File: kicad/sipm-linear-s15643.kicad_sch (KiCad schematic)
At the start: 34 parts, among them J1 SSQ-103-01-G-D, U2 S15643

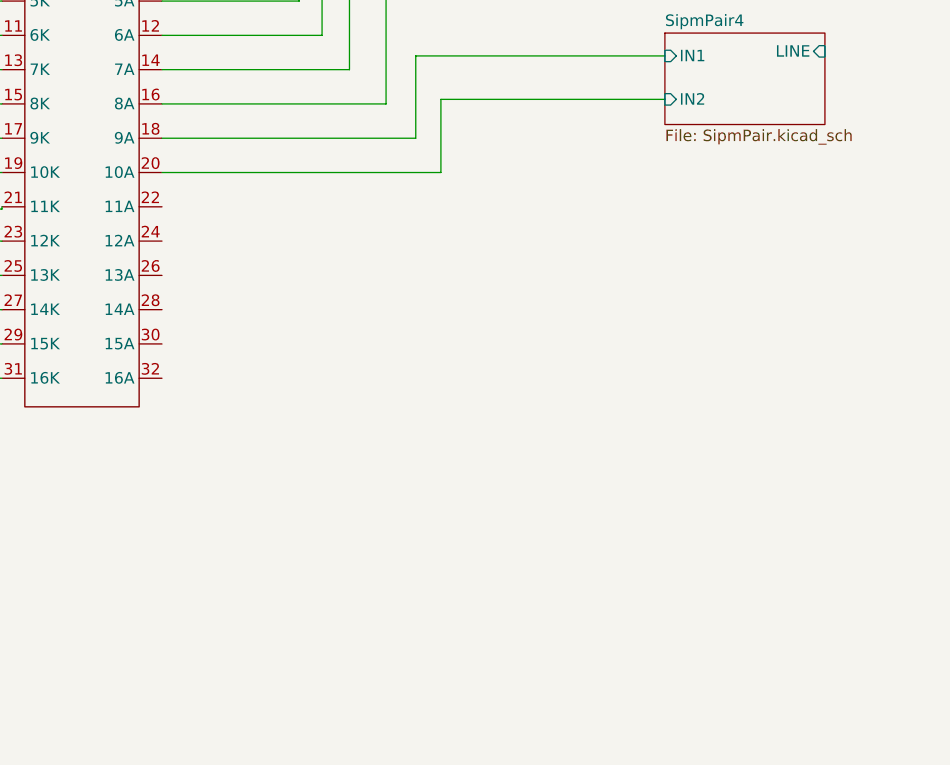
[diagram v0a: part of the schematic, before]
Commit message: Update layout for the new footprint
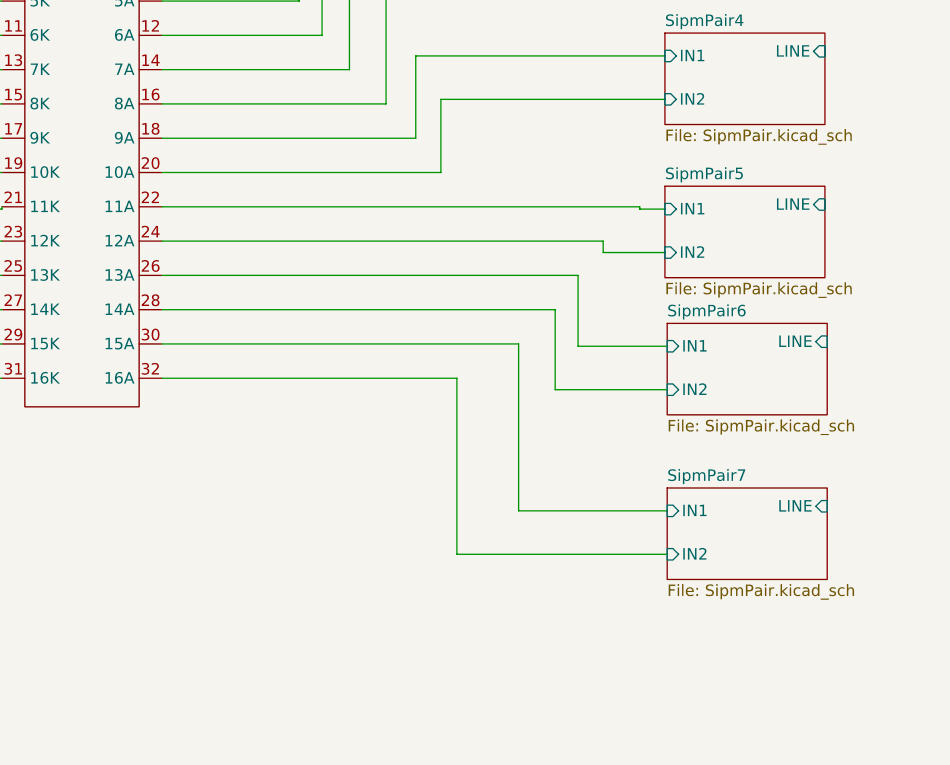
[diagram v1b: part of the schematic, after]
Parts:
- U2: footprint footprints:S15643-N16 -> S13615-1025:AF210729-S14160-x16
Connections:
- net SipmPair5/IN1: now reaches U2.22 (11A)
- net SipmPair5/IN2: now reaches U2.24 (12A)
- net SipmPair6/IN1: now reaches U2.26 (13A)
- net SipmPair6/IN2: now reaches U2.28 (14A)
- net SipmPair7/IN1: now reaches U2.30 (15A)
- net SipmPair7/IN2: now reaches U2.32 (16A)
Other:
- added sheet SipmPair5 (SipmPair.kicad_sch)
- added sheet SipmPair6 (SipmPair.kicad_sch)
- added sheet SipmPair7 (SipmPair.kicad_sch)

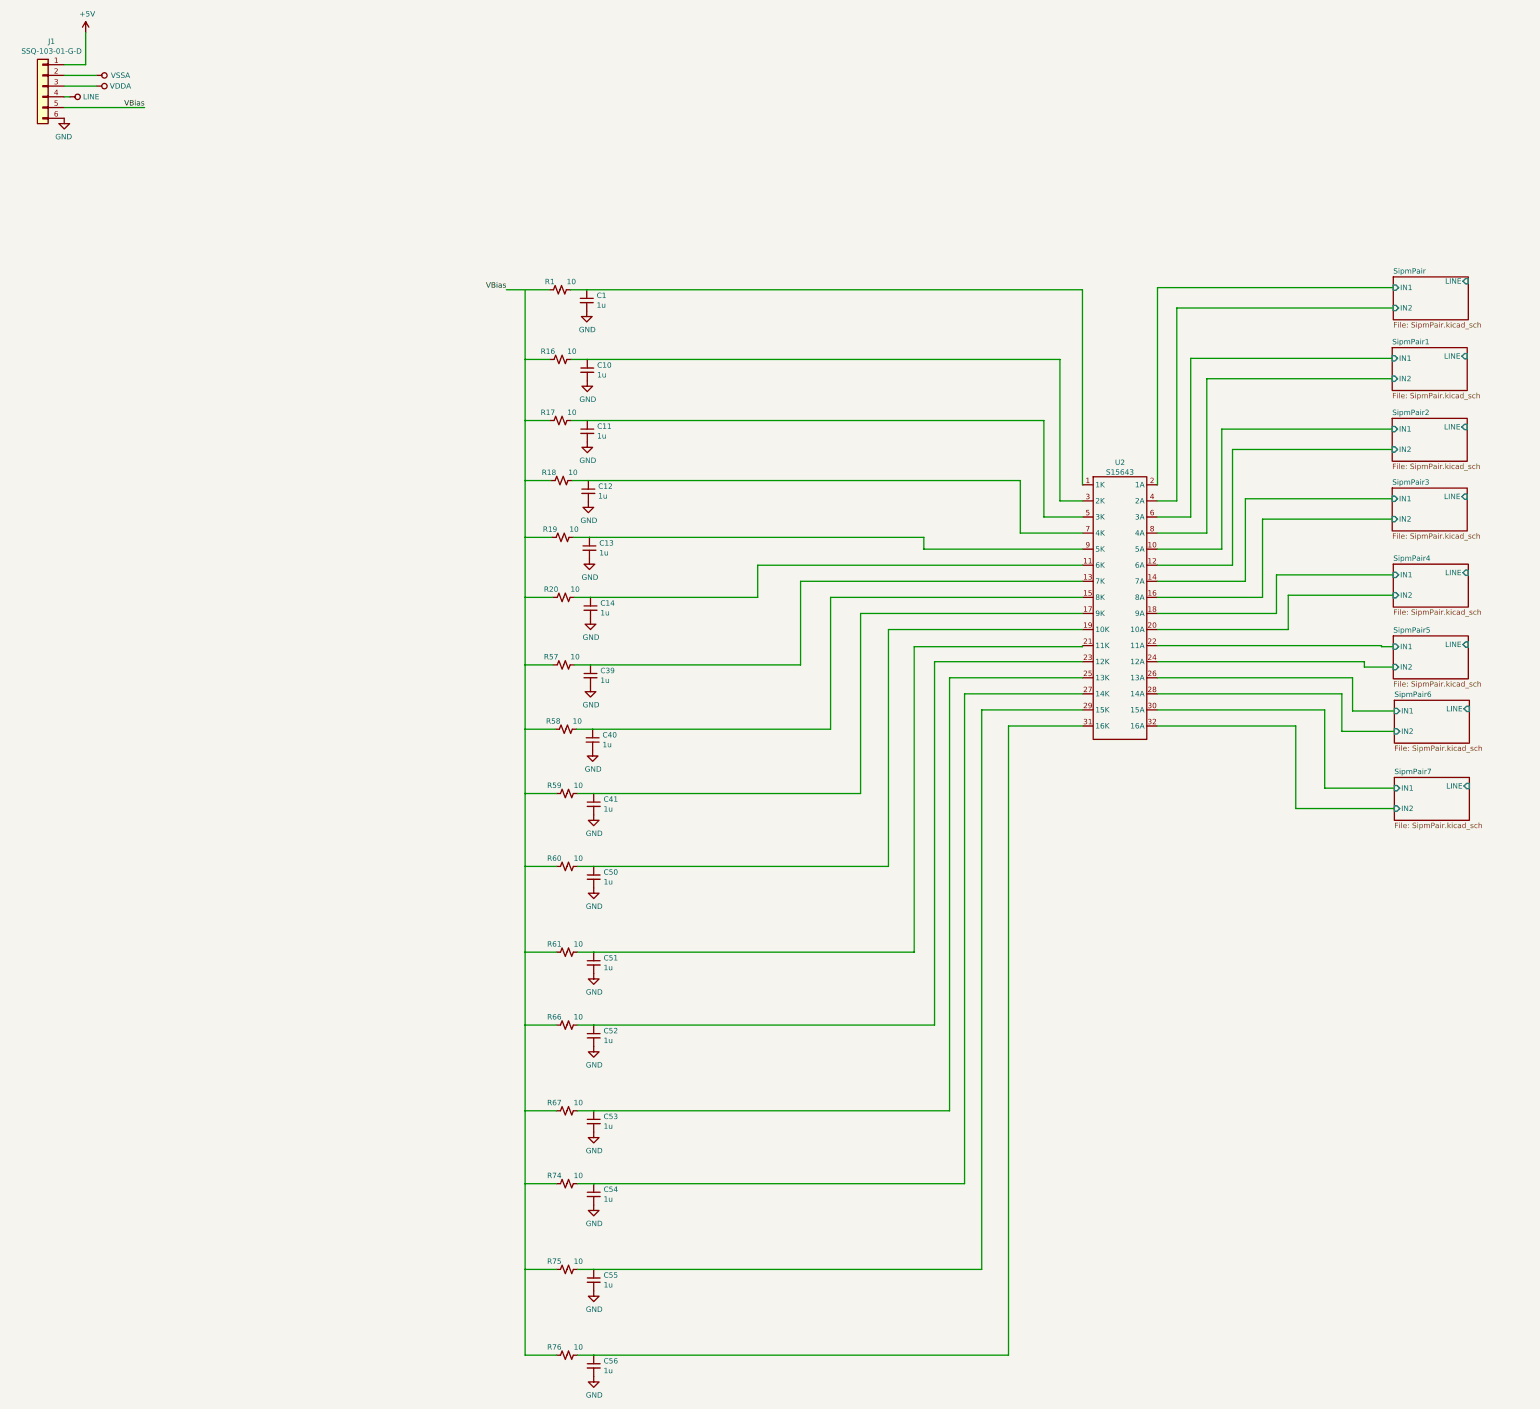
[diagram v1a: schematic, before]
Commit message: Update foot print for the revised hamamatsu part
They only have 2 cathode connections.  In addition, add a second power connector, since at least two power supplies are going to be needed.
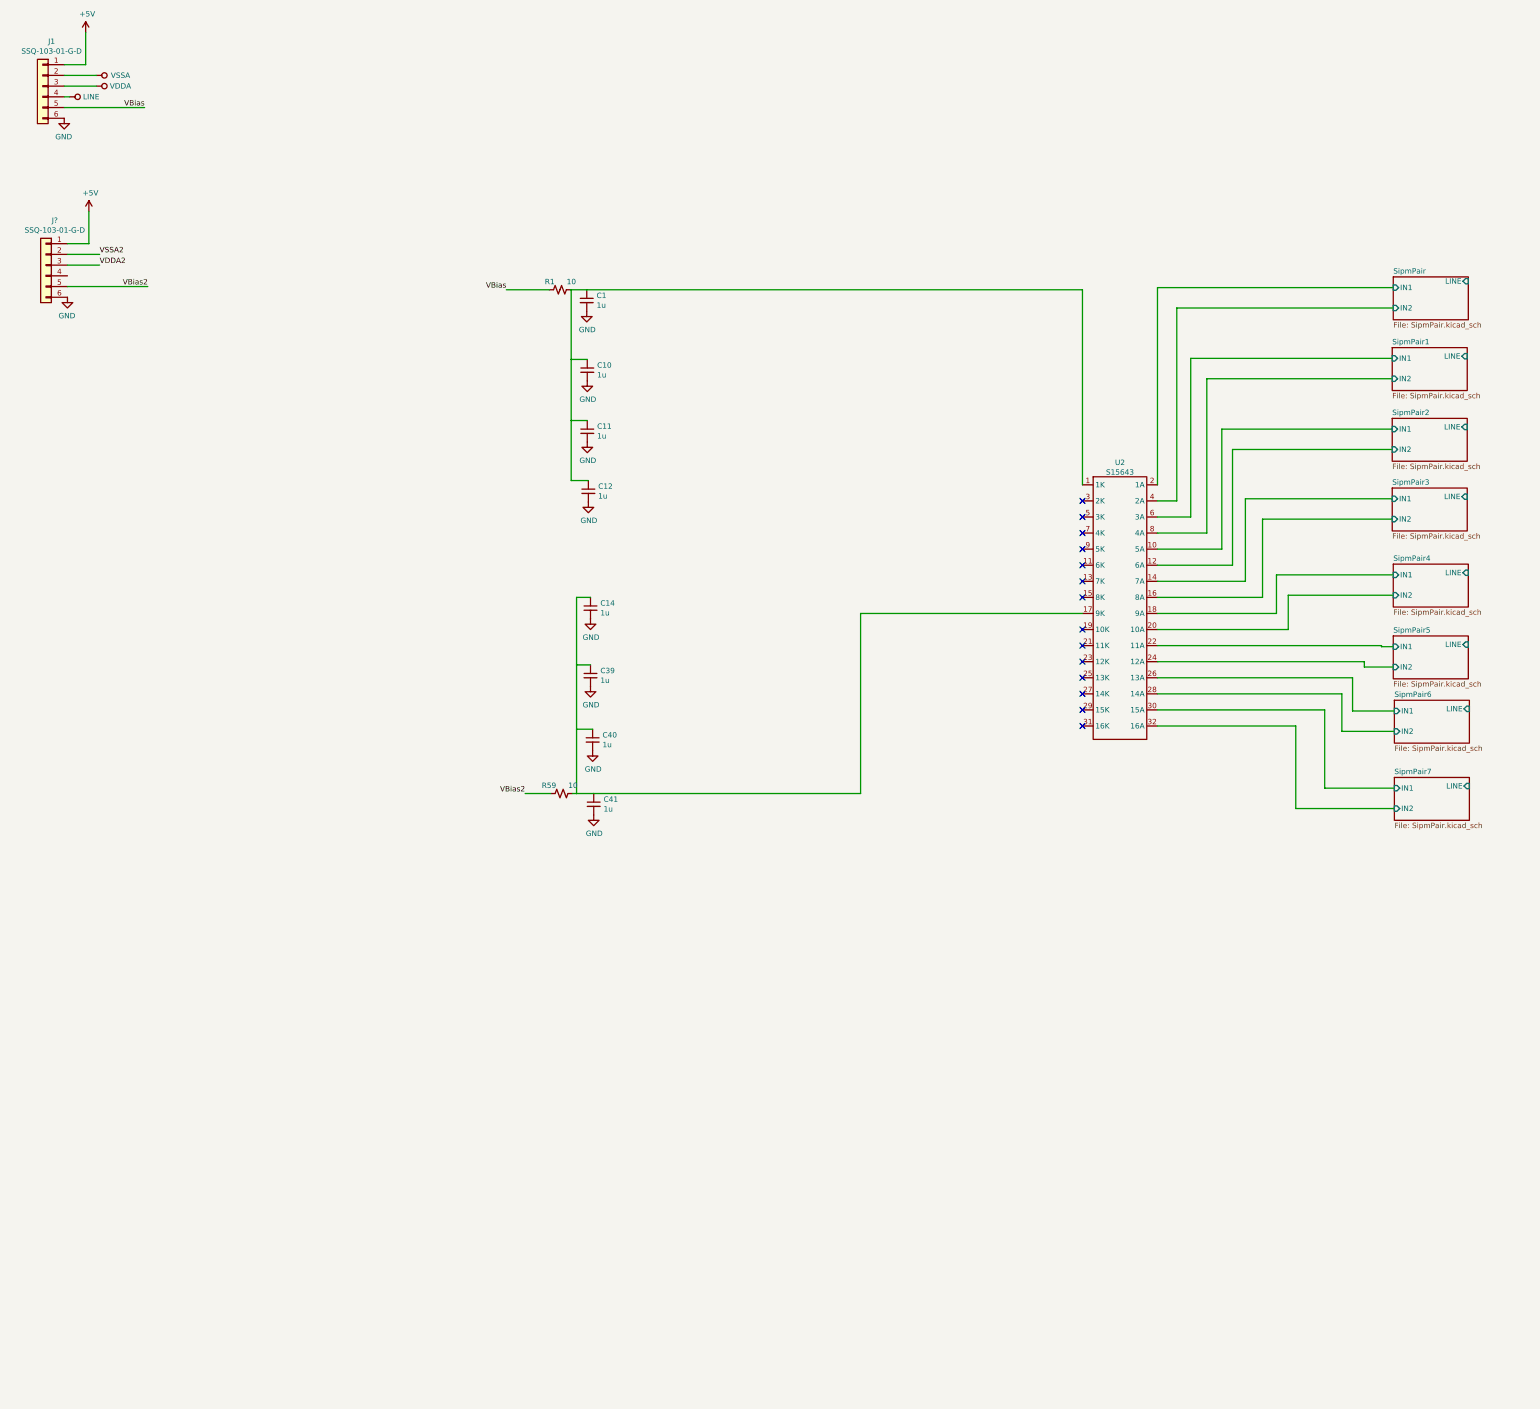
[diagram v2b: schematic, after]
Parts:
- removed C13, C50, C51, C52, C53, C54, C55, C56: 1u, Capacitor_SMD:C_0805_2012Metric, symbol Device:C_Small
- removed R16, R17, R18, R19, R20, R57, R58, R60, R61, R66, R67, R74, R75, R76: 10, R_0402_1005Metric, symbol Device:R_Small_US
- added J?: SSQ-103-01-G-D, footprints:PinHeader_2x03_P2.54mm_Vertical, symbol Connector_Generic:Conn_01x06
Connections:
- net +5V: now also J?.1 (Pin_1)
- net GND: now also J?.6 (Pin_6)
- net at C1.1, R1.2, U2.1 (1K): now also C10.1, C11.1, C12.1
- net at U2.11 (6K): no longer C14.1
- net at U2.13 (7K): no longer C39.1
- net at U2.15 (8K): no longer C40.1
- net at C41.1, R59.2, U2.17 (9K): now also C14.1, C39.1, C40.1
- net at U2.3 (2K): no longer C10.1
- net at U2.5 (3K): no longer C11.1
- net at U2.7 (4K): no longer C12.1
- net VBias2: now reaches R59.1
- net VBias2: now also J?.5 (Pin_5)
- new net VDDA2: J?.3 (Pin_3)
- new net VSSA2: J?.2 (Pin_2)
- no-connect marks 0 -> 14
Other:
- moved on the sheet: R59

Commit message: Split power rails across two power supplies
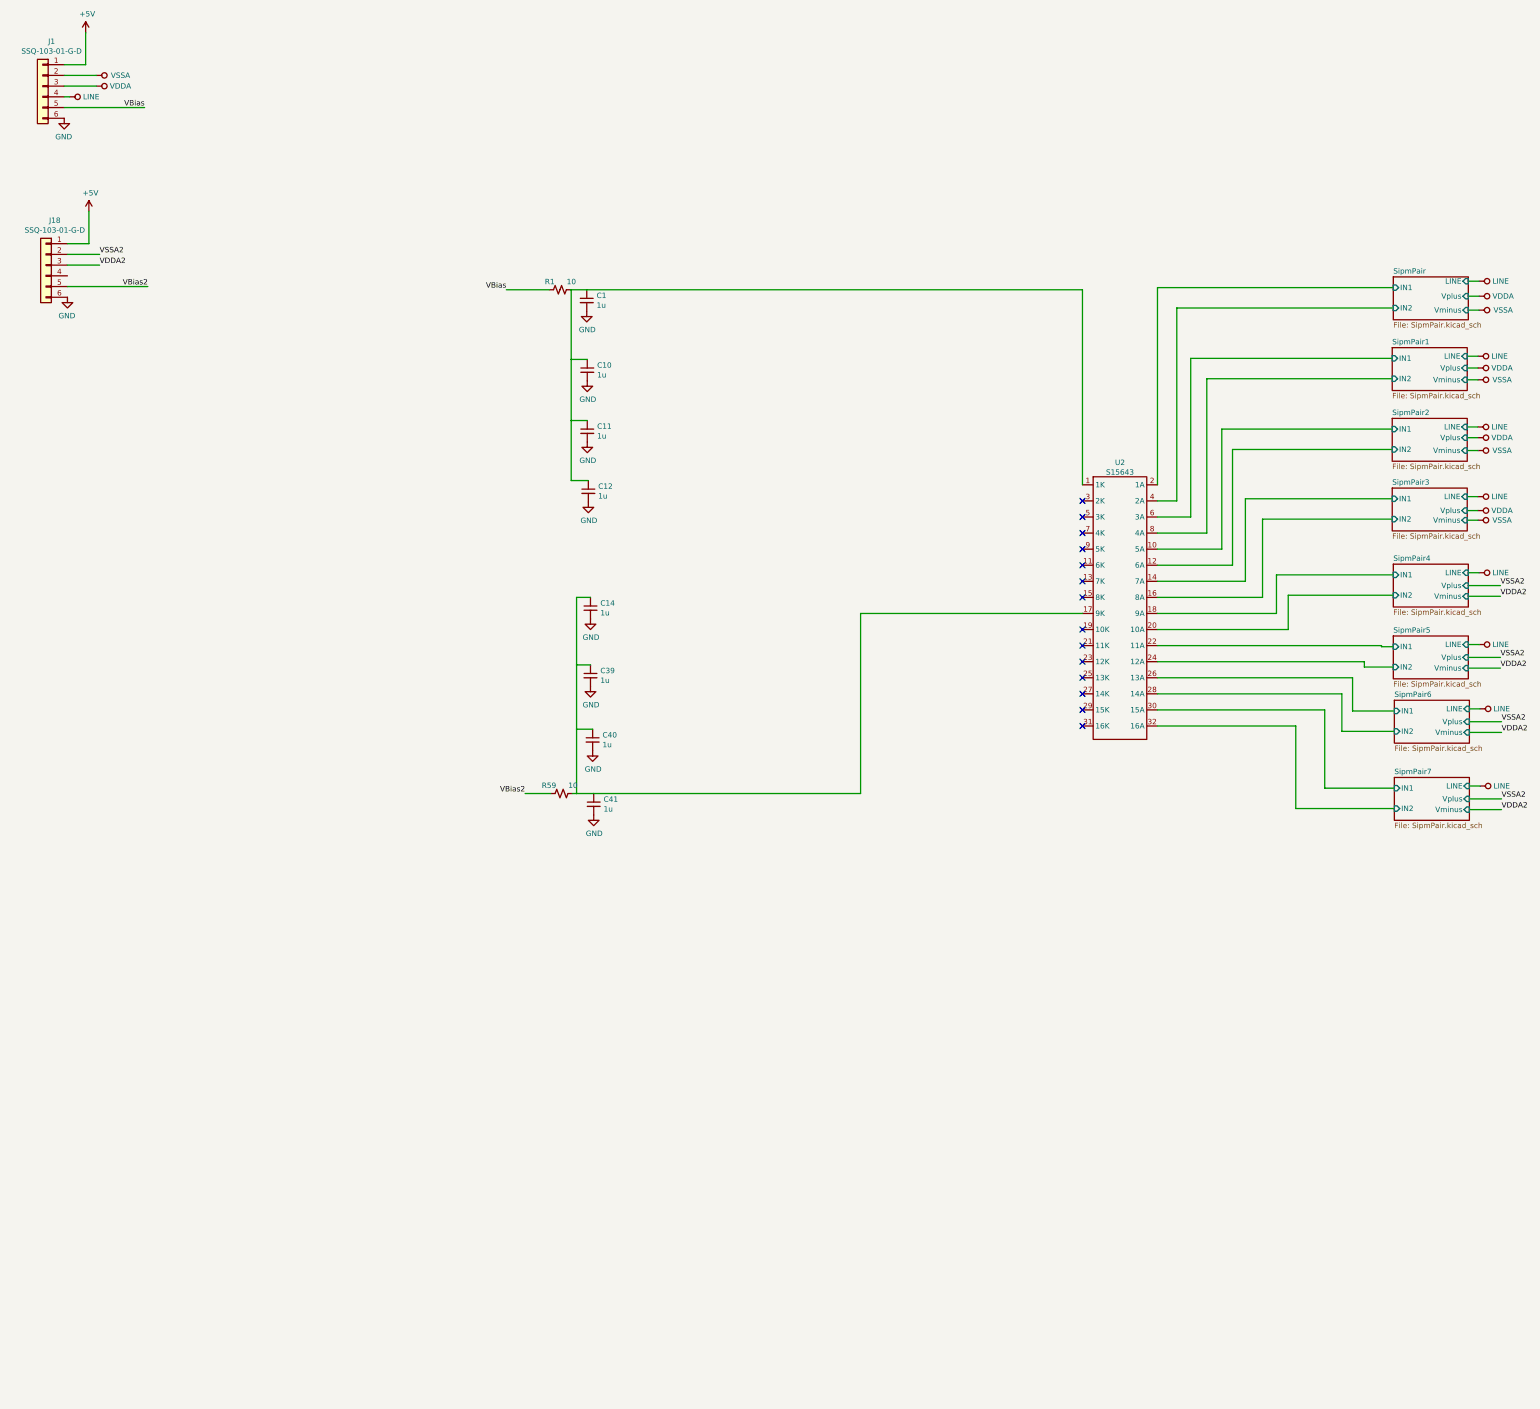
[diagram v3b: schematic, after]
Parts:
- gave numbers to parts that had none: 1
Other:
- sheet SipmPair ports: added Vminus, Vplus; removed none
- sheet SipmPair1 ports: added Vminus, Vplus; removed none
- sheet SipmPair2 ports: added Vminus, Vplus; removed none
- sheet SipmPair3 ports: added Vminus, Vplus; removed none
- sheet SipmPair4 ports: added Vminus, Vplus; removed none
- sheet SipmPair5 ports: added Vminus, Vplus; removed none
- sheet SipmPair6 ports: added Vminus, Vplus; removed none
- sheet SipmPair7 ports: added Vminus, Vplus; removed none
